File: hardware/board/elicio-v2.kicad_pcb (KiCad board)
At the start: 2 copper layers, 38 x 55.2 mm, 68 parts, among them J2 SM02B-SRSS-TB, J3 HDR-3-RA, J4 TC2030-NL, P1 SIG1, P2 SIG2, P3 REF, P4 CHARGE_VBUS, P5 CHARGE_GND, Q1 AO3401A, Q2 2N7002, Q3 2N7002, Q4 2N7002, Q5 2N7002, SW1 4.5x4.5x1.6, U1 MDBT50Q-1MV2, U2 ADS1292IRSMT, U3 BQ25100YFPR, U4 TLV71330PDBVR

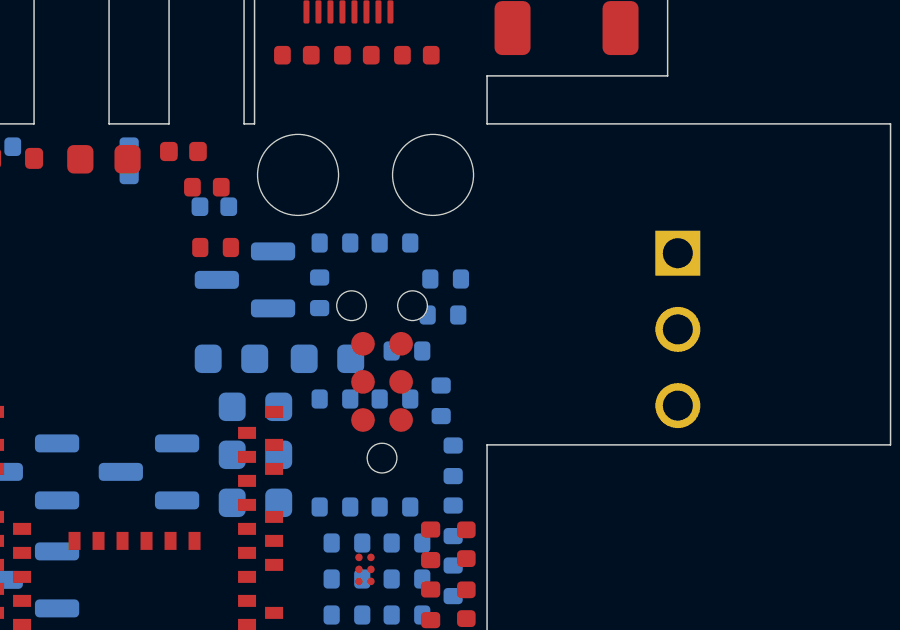
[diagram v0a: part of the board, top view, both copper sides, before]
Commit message: board(v2f): move R24 off J4 NPTH (Q87); flex netclasses in the DSN path
R24 +0.47 mm u clears hole clearance 0.20 on the real TC2030 hole. Zero-track DRC is 0. Default/Contact classes are JLC 1 oz 0.10/0.10 and 0.15/0.20; via 0.70/0.30. scripts/board/route_v2.py checks those class blocks after DSN export.

Co-authored-by: Cursor <cursoragent@cursor.com>
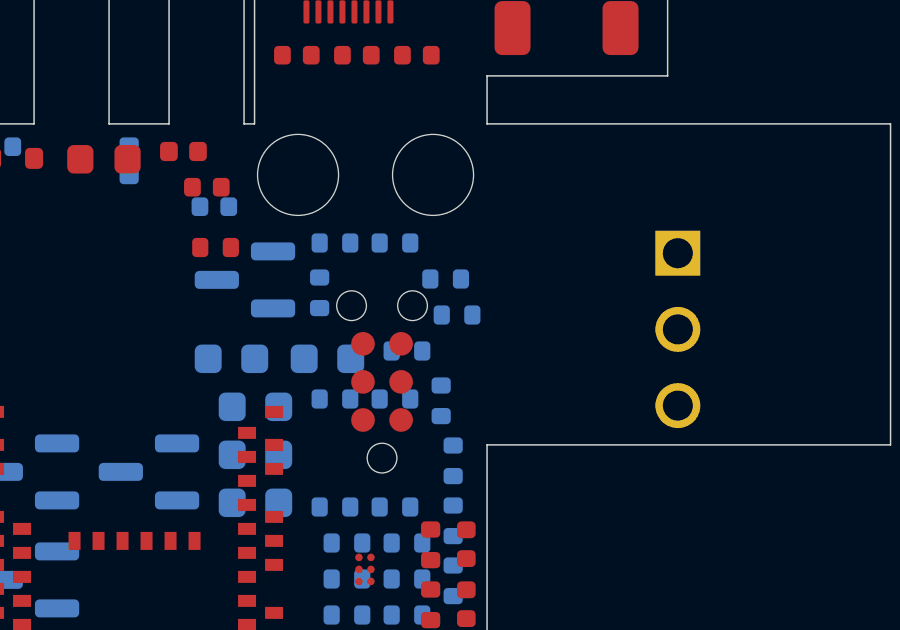
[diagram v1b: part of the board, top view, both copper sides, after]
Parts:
- moved R24 0.47 mm to (18.8, 22.4)

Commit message: board(v2f): lock SIG/REF strip centres and CHARGE tab stubs
DSN class blocks carry Default 100/100 um, Contact 150/200 um, via 700:300 um. Wires are Specctra type fix. Island legs to R1–R3 wait for Freerouting; a scripted manhattan still hits Q84 at L1/D2 and shorts the hang.

Co-authored-by: Cursor <cursoragent@cursor.com>
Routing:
- net SIG2: track 0.00 -> 21.3 mm
- net VBUS: track 0.00 -> 12.8 mm
- net SIG1: track 0.00 -> 10.2 mm
- net GND: track 0.00 -> 5.78 mm
- net REF: track 0.00 -> 5.05 mm

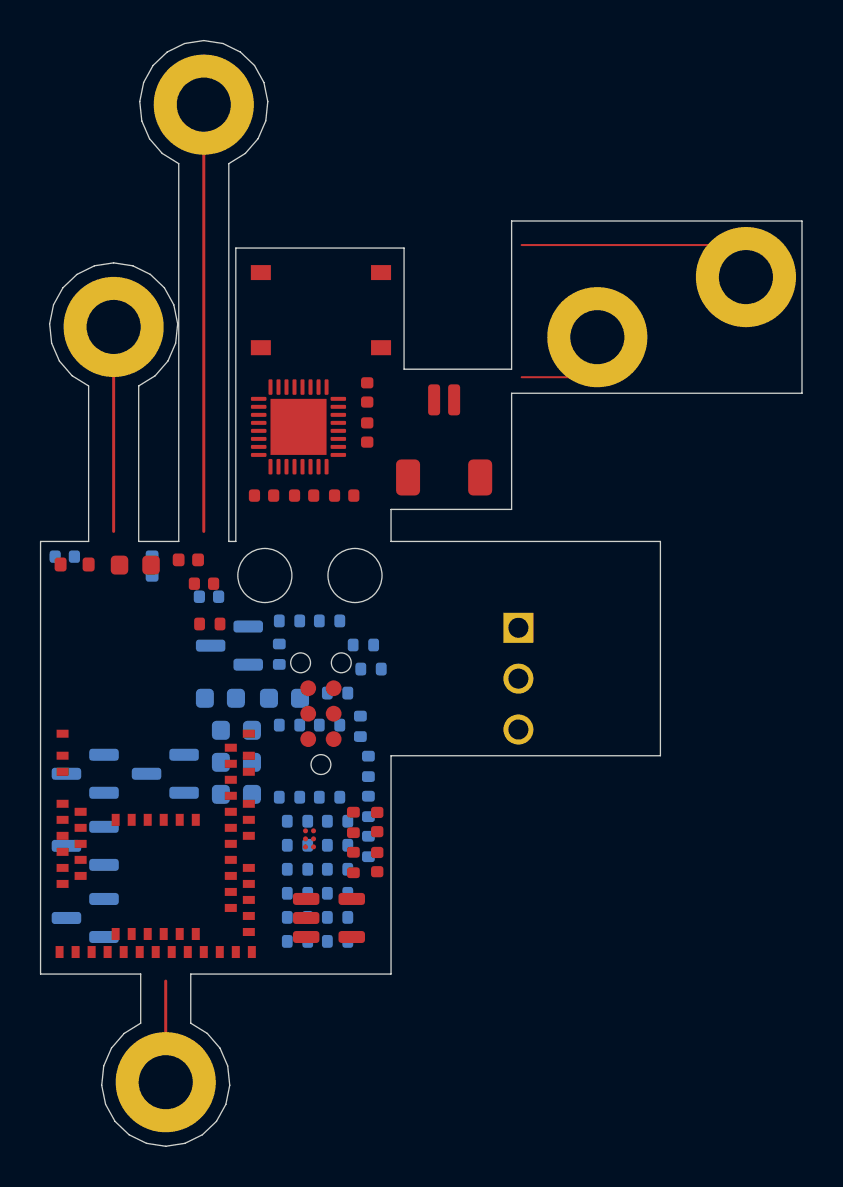
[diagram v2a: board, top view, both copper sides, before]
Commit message: board(v2g): Q88 7×7 lands, pin table v2.1 R24, lock Contact to R1–R3
Shrink tabs/tail_pads to the Ø5 lands plus 1.0 mm. R24 (18.49, 22.57) rot 90 is copper-clean. Locked ring→strip→R1–R3 and charge stubs DRC 0 errors.

Co-authored-by: Cursor <cursoragent@cursor.com>
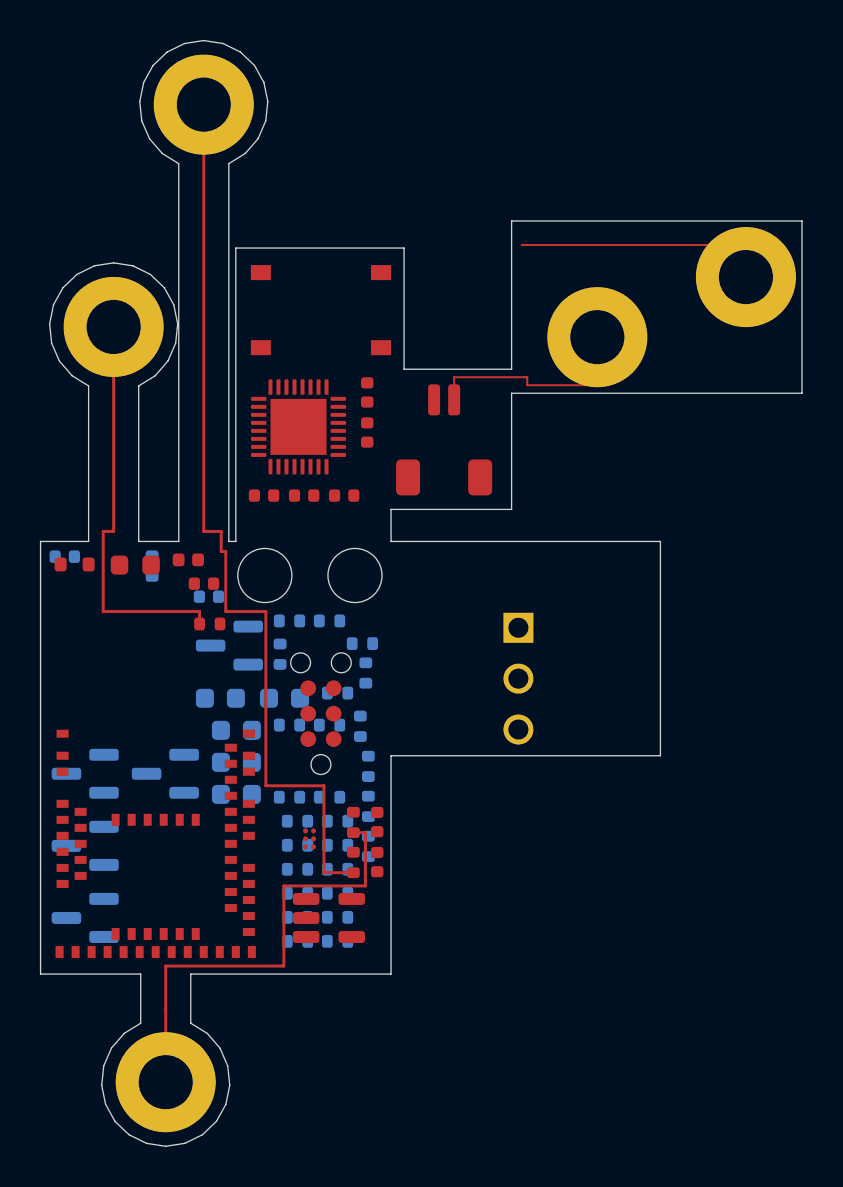
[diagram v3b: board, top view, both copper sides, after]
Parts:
- moved R24 0.33 mm to (18.5, 22.6), turned to 90 degrees
- moved R23 0.09 mm to (18.3, 21.1), turned to 0 degrees
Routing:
- net SIG2: track 21.3 -> 45.8 mm
- net REF: track 5.05 -> 23.0 mm
- net SIG1: track 10.2 -> 20.2 mm
- net GND: track 5.78 -> 11.1 mm

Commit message: board(v2g): Q88 lands, not routed
Contact is locked to R1–R3 and Freerouting imported 421 tracks, but 63 nets stay open. Stop un-shorted; routed is false.

Co-authored-by: Cursor <cursoragent@cursor.com>
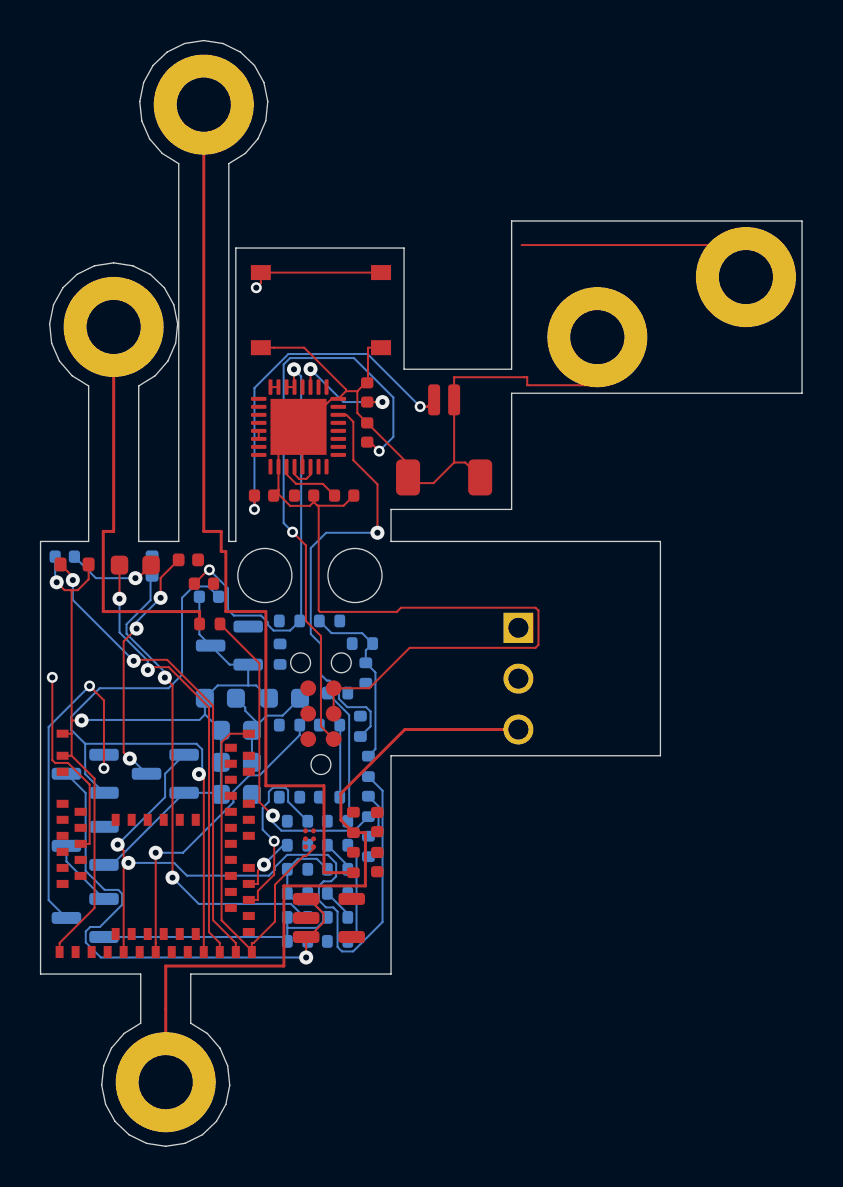
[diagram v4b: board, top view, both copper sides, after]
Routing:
- net GND: track 11.1 -> 177.6 mm, vias 0 -> 2
- net VBAT: track 0.00 -> 54.5 mm, vias 0 -> 3
- net LED_EN: track 0.00 -> 38.8 mm, vias 0 -> 2
- net +VDD: track 0.00 -> 34.5 mm, vias 0 -> 3
- net VBUS: track 12.8 -> 42.0 mm, vias 0 -> 2
- net AFE_VIN: track 0.00 -> 26.1 mm, vias 0 -> 1
- net RLD_FB: track 0.00 -> 24.1 mm, vias 0 -> 2
- net ISET: track 0.00 -> 24.1 mm, vias 0 -> 2
- net DCCH: track 0.00 -> 22.2 mm, vias 0 -> 2
- net AFE_DRDY_AFE: track 0.00 -> 22.1 mm, vias 0 -> 1
- net AFE_GATE: track 0.00 -> 17.9 mm, vias 0 -> 2
- net AFE_IN1P: track 0.00 -> 16.2 mm, vias 0 -> 1
- net AFE_SCLK: track 0.00 -> 15.4 mm, vias 0 -> 1
- net REF: track 23.0 -> 35.4 mm
- net CHG_LED_K: track 0.00 -> 12.3 mm, vias 0 -> 3
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
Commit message: board(v3): RSM land, R9/R10 DNP, Q94 stiffeners, Q97 tests; wait for pin table v3
U2 pads now match ADS1292 4219108/B (0.40 pitch, 0.55 x 0.20, EP 2.8). U3 stays YFP: the inner balls escape radially so there is no BOM swap. R9/R10 are DNP and off the PCB. Stiffeners sit only on a land-free face (count 9). The §5e parser is ready; it does not replace the vendored table until v3 lands.

Co-authored-by: Cursor <cursoragent@cursor.com>
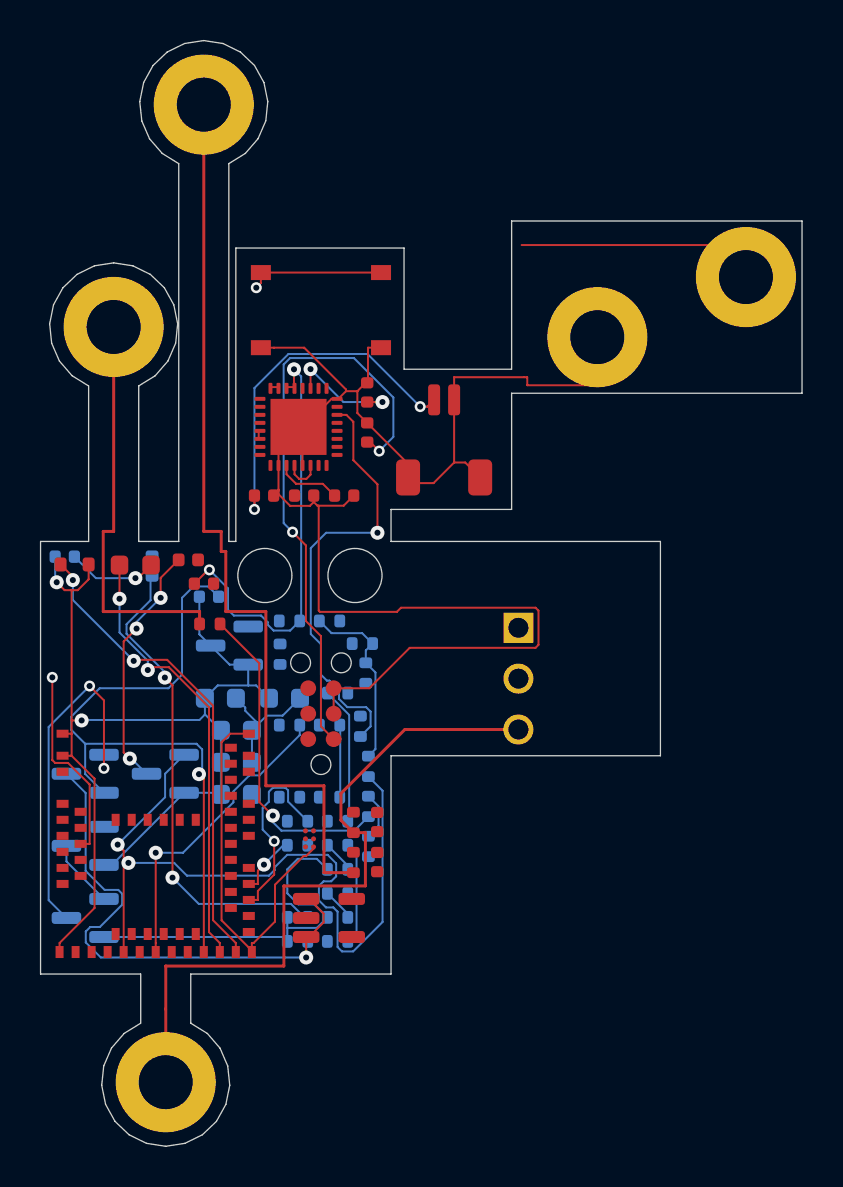
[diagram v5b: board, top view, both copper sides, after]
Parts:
- removed R10, R9: 5.1k, R_0402_1005Metric
- U2: footprint VQFN-32-1EP_4x4mm_P0.4mm_EP2.8x2.8mm -> elicio:Texas_RSM0032
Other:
- board text added: "Eco1 FR4 0.4 U1 RF B.Cu"
- board text added: "Eco1 FR4 0.4 U1 west B.Cu"
- board text added: "Eco1 FR4 0.4 leftover B.Cu face"
- board text added: "Eco2 FR4 0.2 P1"
- board text added: "Eco2 FR4 0.2 P2"
- board text added: "Eco2 FR4 0.2 P3"
- board text added: "Eco2 FR4 0.2 P4"
- board text added: "Eco2 FR4 0.2 P5"
- board text added: "Q94 stiffeners 9 pcs (3xFR4 0.4 + 1xPI 0.1 + 5xFR4 0.2)"
- board text added: "User.1 PI 0.1 F.Cu"
- board text removed: "Eco1 FR4 0.4 #1 parts island"
- board text removed: "Eco1 FR4 0.4 #2 leftover/pocket"

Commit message: board(v3): pin table v3 land, Contact strips locked
Vendor §5e from ab9ce95 (66 rows, Q98 boxes). Rebuild the flat outline
(charge tab at pocket high-u, J3 break-off cut u=22.25). Zero-track DRC 0;
locked ring-to-island Contact. Island rats remain.

Co-authored-by: Cursor <cursoragent@cursor.com>
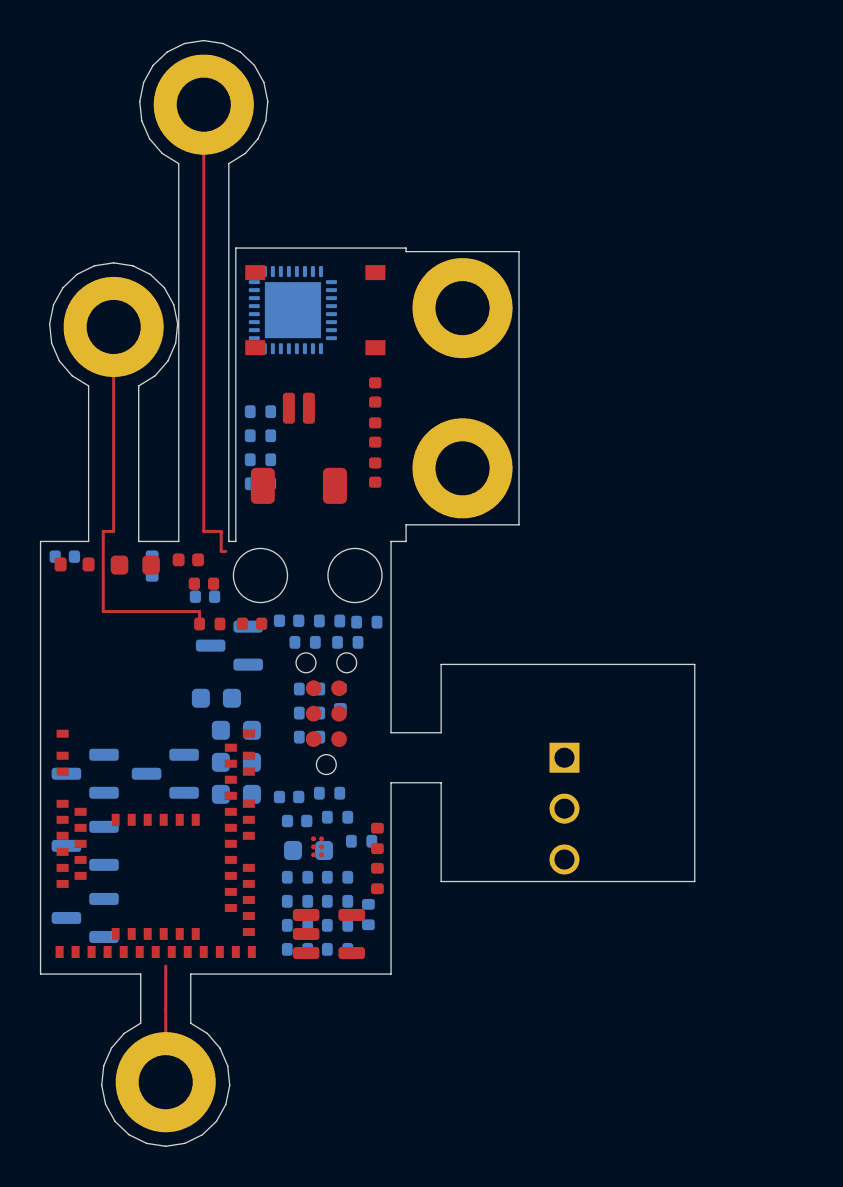
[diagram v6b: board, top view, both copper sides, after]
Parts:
- C10, C11, C12, U2: moved to B.Cu
- moved C3 23.5 mm to (19.0, 8.56)
- moved R25 20.5 mm to (18.6, 34.6)
- moved R21 19.8 mm to (7.82, 17.2), turned to 90 degrees
- moved R30 18.9 mm to (13.2, 13.1), turned to 180 degrees
- moved R29 18.1 mm to (13.2, 11.9), turned to 180 degrees
- moved R28 17.4 mm to (13.2, 10.7), turned to 180 degrees
- moved R27 16.5 mm to (13.2, 9.52), turned to 180 degrees
- moved C13 16.4 mm to (14.7, 28.8)
- moved C10 14.3 mm to (3.46, 16.8), turned to 180 degrees
- moved P4 14.2 mm to (23.3, 4.35)
- moved C11 13.0 mm to (10.5, 18.8), turned to 180 degrees
- moved R4 12.8 mm to (15.1, 32.8)
- moved R22 12.1 mm to (17.2, 23.8), turned to 90 degrees
- moved C14 12.0 mm to (15.1, 30.0)
- moved C2 11.7 mm to (12.8, 20.1), turned to 0 degrees
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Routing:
- net GND: track 177.6 -> 0.00 mm, vias 2 -> 0
- net VBAT: track 54.5 -> 0.00 mm, vias 3 -> 0
- net VBUS: track 42.0 -> 0.00 mm, vias 2 -> 0
- net LED_EN: track 38.8 -> 0.00 mm, vias 2 -> 0
- net +VDD: track 34.5 -> 0.00 mm, vias 3 -> 0
- net REF: track 35.4 -> 5.80 mm
- net AFE_VIN: track 26.1 -> 0.00 mm, vias 1 -> 0
- net RLD_FB: track 24.1 -> 0.00 mm, vias 2 -> 0
- net ISET: track 24.1 -> 0.00 mm, vias 2 -> 0
- net SIG2: track 45.8 -> 23.4 mm
- net DCCH: track 22.2 -> 0.00 mm, vias 2 -> 0
- net AFE_DRDY_AFE: track 22.1 -> 0.00 mm, vias 1 -> 0
- net AFE_GATE: track 17.9 -> 0.00 mm, vias 2 -> 0
- net AFE_IN1P: track 16.2 -> 0.00 mm, vias 1 -> 0
- net AFE_SCLK: track 15.4 -> 0.00 mm, vias 1 -> 0
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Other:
- board size 38 x 55.2 mm -> 32.7 x 55.2 mm
- board text added: "CHARGE TAB Q90"
- board text added: "J3 BREAK-OFF"
- board text added: "J3 CUT u=22.25"
- board text removed: "CHARGE TAB Q86"

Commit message: wip(WP12i): v3 land locked; hand_route interrupted
Pin table v3 is pinned and Contact strips are locked. A* on island
rats failed DRC. VBUS/nRESET tracks from an interrupted run sit on
the board; DRC was not re-run.

Co-authored-by: Cursor <cursoragent@cursor.com>
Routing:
- net VBUS: track 0.00 -> 31.1 mm, vias 0 -> 2
- net nRESET: track 0.00 -> 7.21 mm, vias 0 -> 2
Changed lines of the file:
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@@
+	)
+	(segment
+		(start 18.96 9.04)
+		(end 18.95 8.79)
+		(width 0.1)
+		(layer "F.Cu")
+		(net "VBUS")
+	)
+	(segment
+		(start 3.25 17.15)
+		(end 3.45 17.39)
+		(width 0.1)
+		(layer "F.Cu")
+		(net "VBUS")
+	)
+	(via
+		(at 3.45 17.39)
+		(size 0.55)
+		(drill 0.3)
+		(layers "F.Cu" "B.Cu")
+		(net "VBUS")
+	)
+	(via
+		(at 18.95 8.79)
+		(size 0.55)
+		(drill 0.3)
+		(layers "F.Cu" "B.Cu")
+		(net "VBUS")
+	)
+	(segment
+		(start 23.32 4.35)
+		(end 23.15 4.59)
+		(width 0.1)
+		(layer "B.Cu")
+		(net "VBUS")
+	)
+	(segment
+		(start 12.55 24.29)
+		(end 14.55 24.29)
+		(width 0.1)
+		(layer "B.Cu")
+		(net "VBUS")
+	)
+	(segment
+		(start 14.55 24.29)
+		(end 14.55 23.99)
+		(width 0.1)
+		(layer "B.Cu")
+		(net "VBUS")
+	)
+	(segment
+		(start 3.45 17.39)
+		(end 3.45 23.09)
+		(width 0.1)
+		(layer "B.Cu")
+		(net "VBUS")
+	)
+	(segment
+		(start 11.05 24.59)
+		(end 12.55 24.59)
+		(width 0.1)
+		(layer "B.Cu")
+		(net "VBUS")
+	)
+	(segment
+		(start 18.95 4.59)
+		(end 18.95 8.79)
+		(width 0.1)
+		(locked yes)
+		(layer "B.Cu")
+		(net "VBUS")
+	)
+	(segment
+		(start 16.85 23.99)
+		(end 16.85 24.09)
+		(width 0.1)
+		(layer "B.Cu")
+		(net "VBUS")
+	)
+	(segment
+		(start 16.85 24.09)
+		(end 17.05 24.09)
+		(width 0.1)
+		(layer "B.Cu")
+		(net "VBUS")
+	)
+	(segment
+		(start 12.55 24.59)
+		(end 12.55 24.29)
+		(width 0.1)
+		(layer "B.Cu")
+		(net "VBUS")
+	)
+	(segment
+		(start 11.05 23.09)
+		(end 11.05 24.59)
+		(width 0.1)
+		(layer "B.Cu")
+		(net "VBUS")
+	)
+	(segment
+		(start 14.55 23.99)
+		(end 16.85 23.99)
+		(width 0.1)
+		(layer "B.Cu")
+		(net "VBUS")
+	)
+	(segment
+		(start 3.45 23.09)
+		(end 11.05 23.09)
+		(width 0.1)
+		(layer "B.Cu")
+		(net "VBUS")
+	)
+	(segment
+		(start 23.15 4.59)
+		(end 18.95 4.59)
+		(width 0.1)
+		(locked yes)
+		(layer "B.Cu")
+		(net "VBUS")
+	)
+	(segment
+		(start 17.22 24.34)
+		(end 17.05 24.09)
+		(width 0.1)
+		(layer "B.Cu")
+		(net "VBUS")
 	)
 	(segment
@@
 		(net "REF")
 	)
+	(segment
+		(start 18.97 2.575)
+		(end 18.75 2.39)
+		(width 0.1)
+		(layer "F.Cu")
+		(net "nRESET")
+	)
+	(segment
+		(start 12.97 2.575)
+		(end 12.85 2.39)
+		(width 0.1)
+		(layer "F.Cu")
+		(net "nRESET")
+	)
+	(via
+		(at 12.85 2.39)
+		(size 0.55)
+		(drill 0.3)
+		(layers "F.Cu" "B.Cu")
+		(net "nRESET")
+	)
+	(via
+		(at 18.75 2.39)
+		(size 0.55)
+		(drill 0.3)
+		(layers "F.Cu" "B.Cu")
+		(net "nRESET")
+	)
+	(segment
+		(start 16.85 2.39)
+		(end 16.85 1.99)
+		(width 0.1)
+		(layer "B.Cu")
+		(net "nRESET")
+	)
+	(segment
+		(start 18.75 2.39)
+		(end 16.85 2.39)
+		(width 0.1)
+		(layer "B.Cu")
+		(net "nRESET")
+	)
+	(segment
+		(start 12.85 1.99)
+		(end 12.85 2.39)
+		(width 0.1)
+		(layer "B.Cu")
+		(net "nRESET")
+	)
+	(segment
+		(start 16.85 1.99)
+		(end 12.85 1.99)
+		(width 0.1)
+		(layer "B.Cu")
+		(net "nRESET")
+	)
 	(zone
